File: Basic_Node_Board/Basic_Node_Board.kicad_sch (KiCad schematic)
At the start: 0 parts

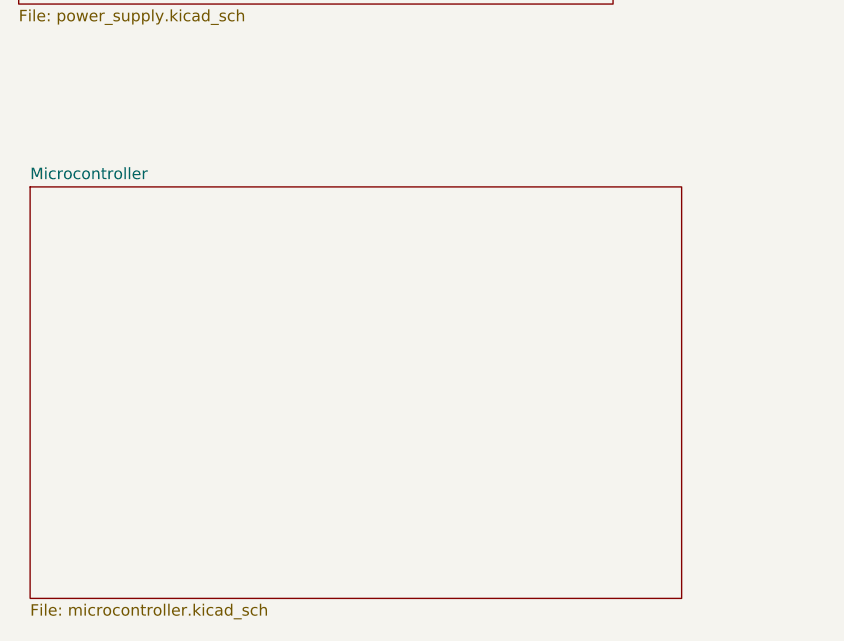
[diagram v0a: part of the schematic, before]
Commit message: Add INA220 current sensor to schematic
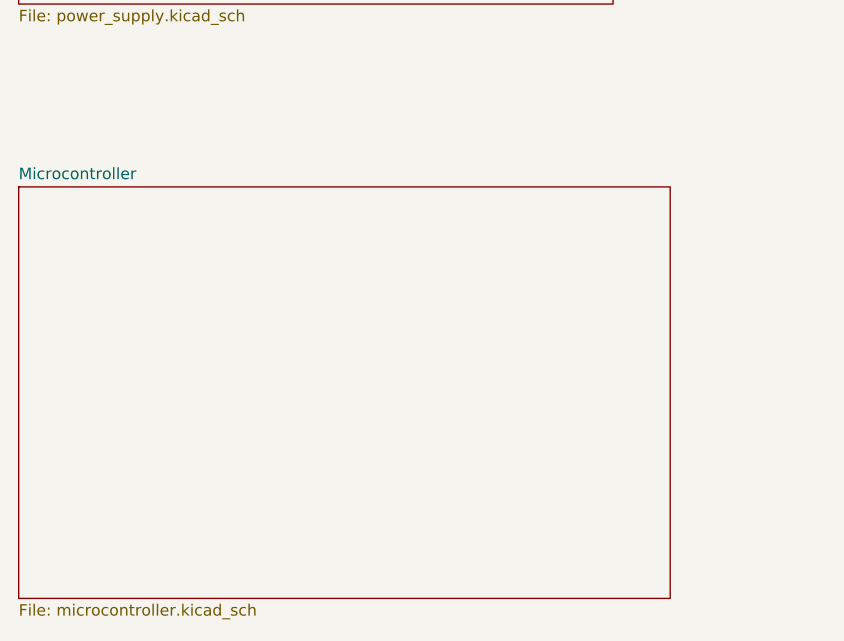
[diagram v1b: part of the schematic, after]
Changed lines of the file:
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@@
 	)
 	(sheet
-		(at 33.02 88.9)
+		(at 31.75 88.9)
 		(size 72.39 45.72)
 		(fields_autoplaced yes)
@@
 		)
 		(property "Sheetname" "Microcontroller"
-			(at 33.02 88.1884 0)
+			(at 31.75 88.1884 0)
 			(effects
 				(font
@@
 		)
 		(property "Sheetfile" "microcontroller.kicad_sch"
-			(at 33.02 135.2046 0)
+			(at 31.75 135.2046 0)
 			(effects
 				(font
